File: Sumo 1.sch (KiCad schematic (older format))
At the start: 17 parts, among them J1 Trinket_Pro_5V, J2 SENSOR_CONN, J3 SENSOR_CONN, J4 SENSOR_CONN, M1 Motor_Connection, M2 Motor_Connection, M3 Motor_Connection, M4 Motor_Connection, U1 TB6612FNG

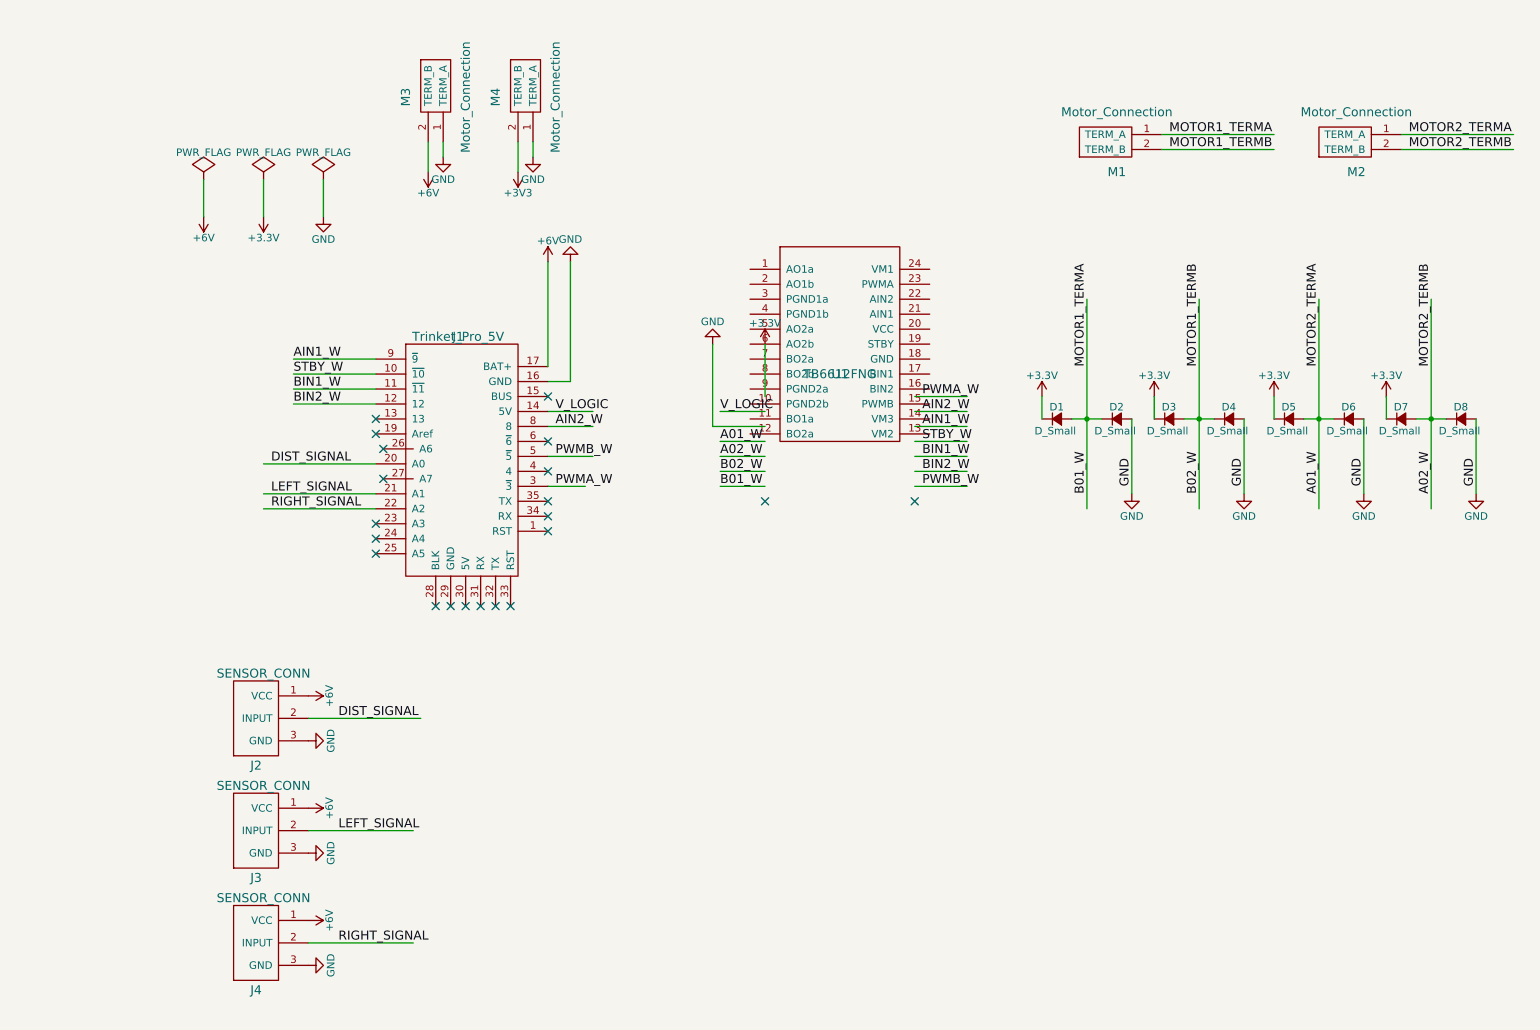
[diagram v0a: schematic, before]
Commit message: First spin using bare SMT TB6612FNG.
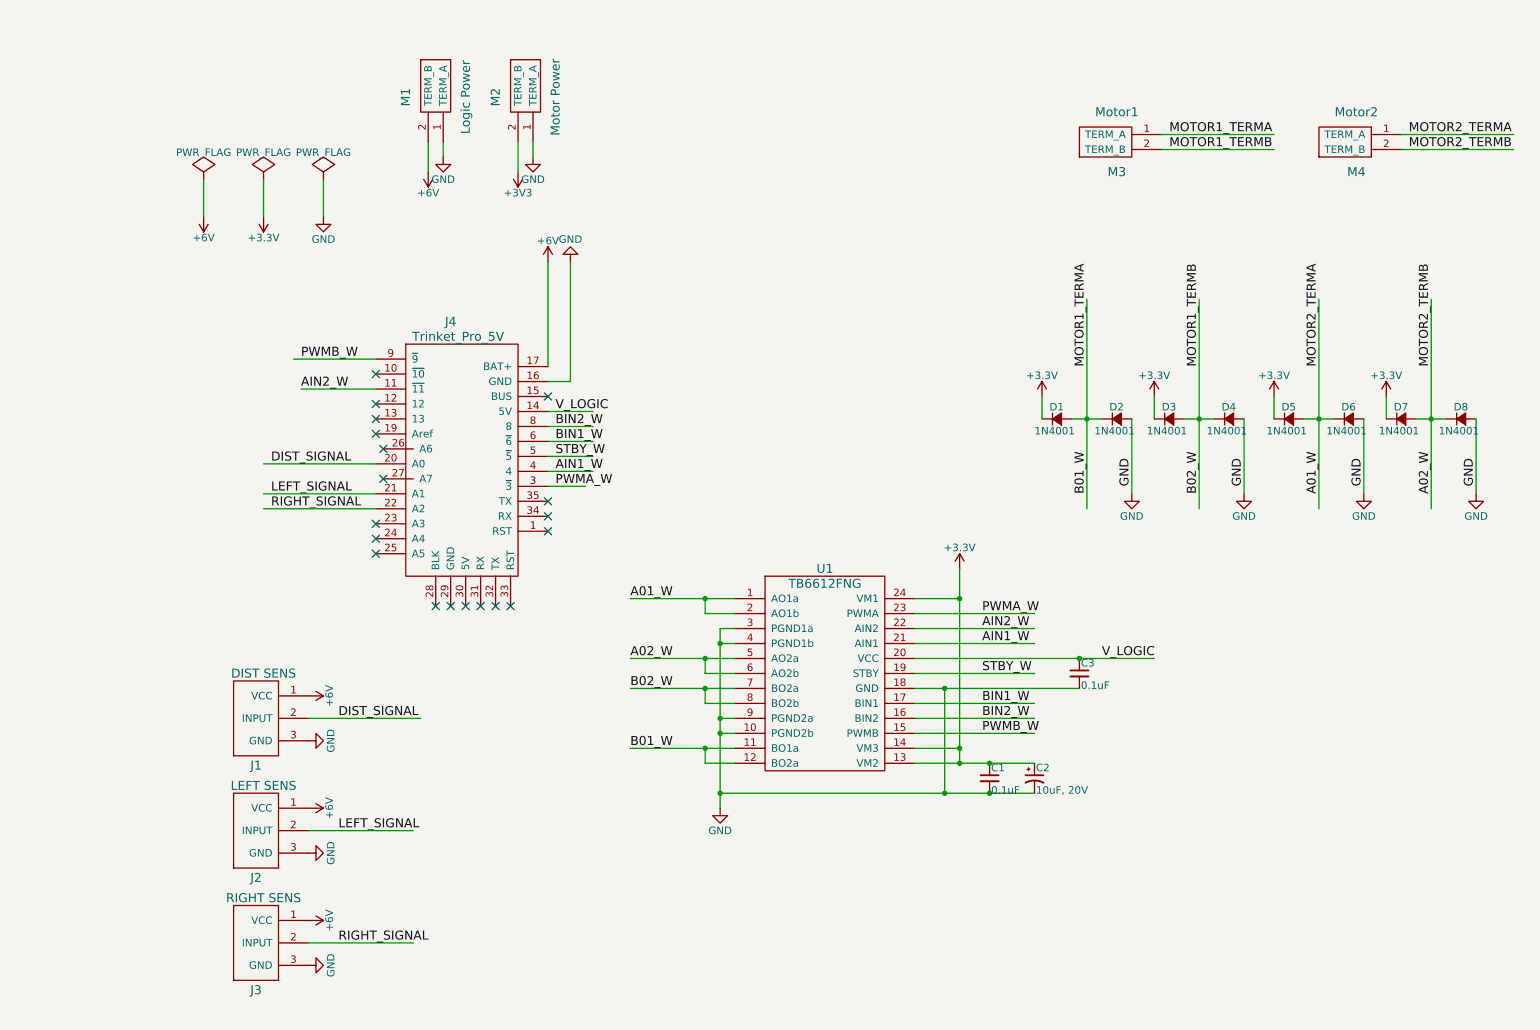
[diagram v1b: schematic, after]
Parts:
- added C1, C3: 0.1uF, Capacitors_SMD:C_0603_HandSoldering, symbol C_Small
- added C2: 10uF, 20V, Capacitors_Tantalum_SMD:TantalC_SizeC_EIA-6032_HandSoldering, symbol CP1_Small
- D1, D2, D3, D4, D5, D6, D7, D8: value D_Small -> 1N4001; footprint ArduinoFootprints:S1BB_rectifier_diode -> Diodes_ThroughHole:Diode_DO-35_SOD27_Horizontal_RM10
- J1: renamed from J2; value SENSOR_CONN -> DIST SENS
- J2: renamed from J3; value SENSOR_CONN -> LEFT SENS
- J3: renamed from J4; value SENSOR_CONN -> RIGHT SENS
- M1: renamed from M3; value Motor_Connection -> Logic Power; footprint Connect:BARREL_JACK -> Terminal_Blocks:TerminalBlock_Pheonix_PT-3.5mm_2pol
- M2: renamed from M4; value Motor_Connection -> Motor Power; footprint Connect:BARREL_JACK -> Terminal_Blocks:TerminalBlock_Pheonix_PT-3.5mm_2pol
- M3: renamed from M1; value Motor_Connection -> Motor1; footprint Pin_Headers:Pin_Header_Straight_1x02 -> Terminal_Blocks:TerminalBlock_Pheonix_PT-3.5mm_2pol
- M4: renamed from M2; value Motor_Connection -> Motor2; footprint Pin_Headers:Pin_Header_Straight_1x02 -> Terminal_Blocks:TerminalBlock_Pheonix_PT-3.5mm_2pol
- U1: footprint ArduinoFootprints:TB6612FNG_motor_driver -> ArduinoFootprints:TB6612FNG
- renumbered J1 to J4
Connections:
- wire segments 59 -> 76
- no-connect marks 21 -> 19

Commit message: New spin!
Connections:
- wire segments 76 -> 79
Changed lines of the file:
@@
-$EndComp
-$Comp
-L +6V #PWR016
-U 1 1 5782A1AA
-P 2450 5150
-F 0 "#PWR016" H 2450 5000 50  0001 C CNN
-F 1 "+6V" H 2450 5290 50  0000 C CNN
-F 2 "" H 2450 5150 50  0000 C CNN
-F 3 "" H 2450 5150 50  0000 C CNN
-	1    2450 5150
-	0    1    1    0
-$EndComp
-$Comp
-L +6V #PWR017
-U 1 1 5782A1D8
-P 2450 5900
-F 0 "#PWR017" H 2450 5750 50  0001 C CNN
-F 1 "+6V" H 2450 6040 50  0000 C CNN
-F 2 "" H 2450 5900 50  0000 C CNN
-F 3 "" H 2450 5900 50  0000 C CNN
-	1    2450 5900
-	0    1    1    0
-$EndComp
-$Comp
-L +6V #PWR018
-U 1 1 5782A206
-P 2450 6650
-F 0 "#PWR018" H 2450 6500 50  0001 C CNN
-F 1 "+6V" H 2450 6790 50  0000 C CNN
-F 2 "" H 2450 6650 50  0000 C CNN
-F 3 "" H 2450 6650 50  0000 C CNN
-	1    2450 6650
-	0    1    1    0
 $EndComp
 $Comp
@@
 Wire Wire Line
 	2150 1950 2150 1700
+Wire Wire Line
+	2450 5150 3200 5150
+Wire Wire Line
+	2450 5900 3150 5900
+Wire Wire Line
+	2450 6650 3150 6650
+Text Label 2650 5150 0    60   ~ 0
+V_LOGIC
+Text Label 2650 5900 0    60   ~ 0
+V_LOGIC
+Text Label 2650 6650 0    60   ~ 0
+V_LOGIC
 $EndSCHEMATC

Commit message: Sumo v1 files
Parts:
- removed M4: Motor2, Terminal_Blocks:TerminalBlock_Pheonix_PT-3.5mm_2pol, symbol Motor_Connection
- added C4: 10uF, 20V, Capacitors_ThroughHole:C_Radial_D5_L6_P2.5, symbol CP1_Small
- added M2: Motor2, Terminal_Blocks:TerminalBlock_Pheonix_PT-3.5mm_2pol, symbol Motor_Connection
- added P4: LED1, Pin_Headers:Pin_Header_Straight_1x03, symbol CONN_01X03
- added P5: LED2, Pin_Headers:Pin_Header_Straight_1x02, symbol CONN_01X02
- added XP1: EXP, Pin_Headers:Pin_Header_Straight_1x08, symbol CONN_01X08
- C1, C3: footprint Capacitors_SMD:C_0603_HandSoldering -> Capacitors_ThroughHole:C_Disc_D7.5_P5
- C2: footprint Capacitors_Tantalum_SMD:TantalC_SizeC_EIA-6032_HandSoldering -> Capacitors_ThroughHole:C_Radial_D5_L6_P2.5
- renumbered J4 to J1, M1 to LPWR1, M3 to M1, M2 to MPWR1, J1 to P1, J2 to P2, J3 to P3
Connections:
- net labels added: A01, A02, A4, A5, AIN1, AIN2, AREF, B01, B02, BIN1, BIN2, GND_LOGIC, GND_MOTOR, LED1_GREEN, LED1_RED, LED2, PWMA, PWMB, RST, RX, SENS_DIST, SENS_LEFT, SENS_RIGHT, STBY, TX, V_BAT, V_MOTOR
- net labels removed: +3V3, A01_W, A02_W, AIN1_W, AIN2_W, B01_W, B02_W, BIN1_W, BIN2_W, DIST_SIGNAL, LEFT_SIGNAL, MOTOR1_TERMA, MOTOR1_TERMB, MOTOR2_TERMA, MOTOR2_TERMB, PWMA_W, PWMB_W, RIGHT_SIGNAL, STBY_W
- wire segments 79 -> 120
- no-connect marks 19 -> 11
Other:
- note added: "Bypass capacitors\nmust be close to U1"
- moved on the sheet: C1, C2, D1, D2, D3, D4, J1, LPWR1, M1, MPWR1, P1, P2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
